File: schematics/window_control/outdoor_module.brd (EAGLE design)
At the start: 62.2 x 54.3 mm, 25 parts, among them J1 J_SMD, J10 USBASP_PIN, J2 J_SMD, J3 J_SMD, U5 BMP280 5V module, U6 LM317L, U7 LM358, U8 ATMEGA328P, U9 GY-SGP30

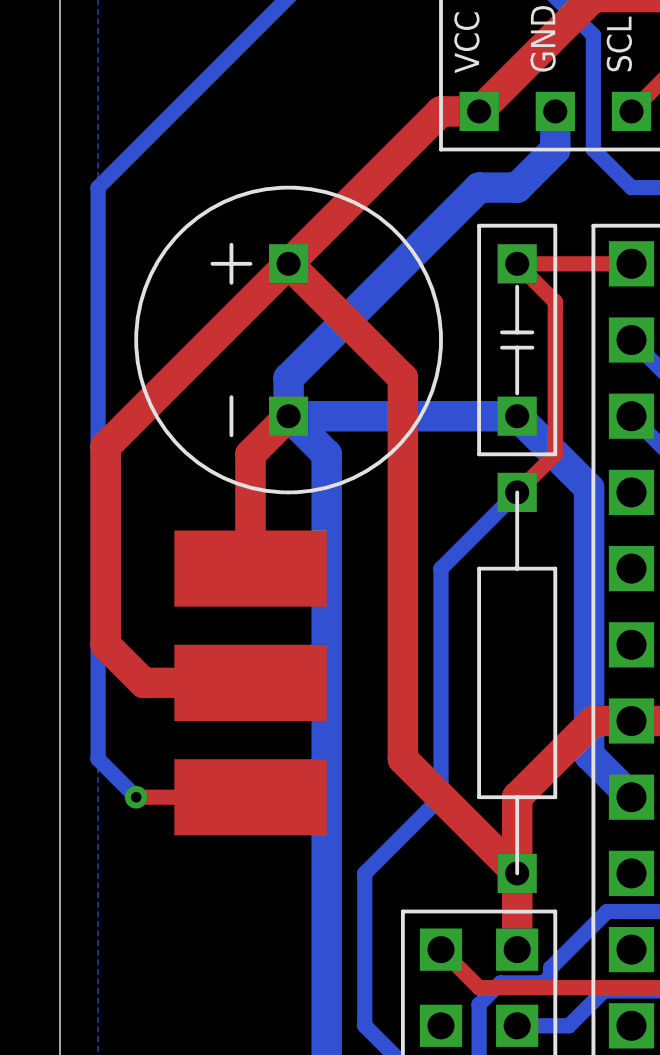
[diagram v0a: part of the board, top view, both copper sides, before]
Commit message: Connectors changed
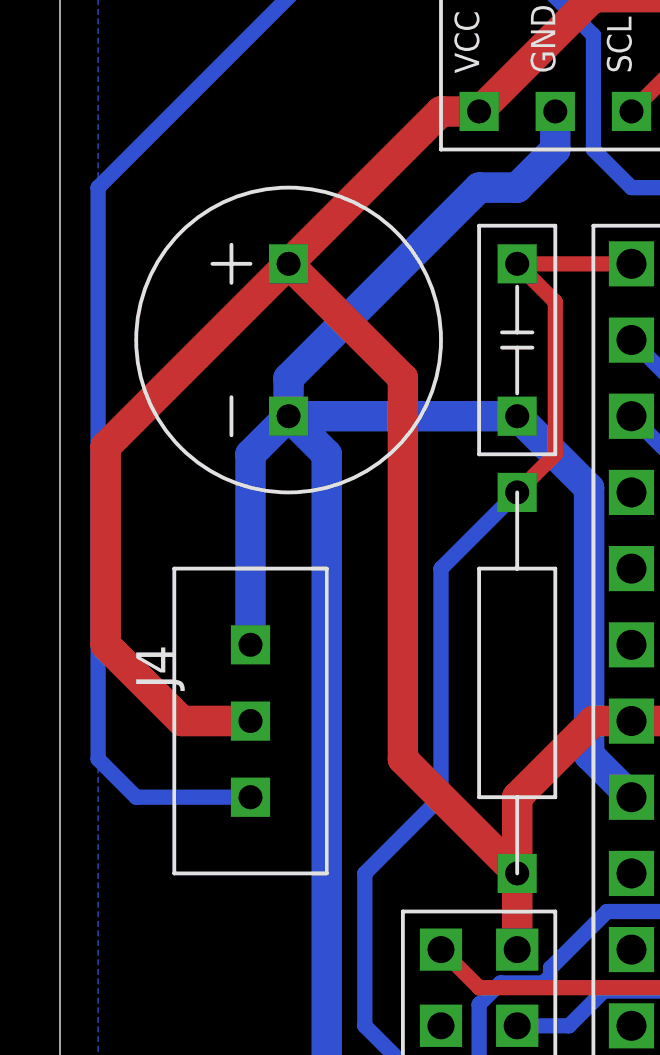
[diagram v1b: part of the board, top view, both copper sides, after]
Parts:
- removed J1, J2, J3: J_SMD, my_devices:J_SMD
- added J4: JST-XH2.54-3P, my_devices:JST-XH254-3P
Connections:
- net OUTDOOR_+5V: now also J4.PIN2; no longer J1.PIN
- net OUTDOOR_DATA_OUT: now also J4.PIN3; no longer J3.PIN
- net OUTDOOR_GND: now also J4.PIN1; no longer J2.PIN
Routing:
- net OUTDOOR_GND: track 216.7 -> 219.1 mm
- net OUTDOOR_+5V: track 121.1 -> 120.4 mm
- net OUTDOOR_DATA_OUT: track 63.4 -> 63.2 mm, vias 1 -> 0
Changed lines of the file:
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@@
 <drawing>
 <settings>
-<setting alwaysvectorfont="yes"/>
+<setting alwaysvectorfont="no"/>
 <setting verticaltext="up"/>
 </settings>
@@
 <element name="C8" library="my_devices" package="C-1" value="0.1 uF" x="124.46" y="-20.32" smashed="yes"/>
 <element name="C9" library="my_devices" package="C-1" value="0.1 uF" x="87.63" y="12.7" smashed="yes" rot="R90"/>
-<element name="J1" library="my_devices" package="J_SMD" value="J_SMD" x="78.74" y="1.27" smashed="yes"/>
 <element name="J10" library="my_devices" package="USBASP_PIN" value="USBASP_PIN" x="86.36" y="-12.7" smashed="yes"/>
-<element name="J2" library="my_devices" package="J_SMD" value="J_SMD" x="78.74" y="5.08" smashed="yes" rot="R180"/>
-<element name="J3" library="my_devices" package="J_SMD" value="J_SMD" x="78.74" y="-2.54" smashed="yes"/>
 <element name="L2" library="my_devices" package="L-EC24" value="EC24-561K, 560 uH" x="124.46" y="20.32" smashed="yes" rot="R270"/>
 <element name="L3" library="my_devices" package="L-EC24" value="EC24-561K, 560 uH" x="110.49" y="1.27" smashed="yes"/>
@@
 <element name="U8" library="my_devices" package="ATMEGA328P" value="ATMEGA328P" x="95.25" y="0" smashed="yes"/>
 <element name="U9" library="my_devices" package="GY-SGP30" value="GY-SGP30" x="106.68" y="20.32" smashed="yes" rot="R90"/>
+<element name="J4" library="my_devices" package="JST-XH254-3P" value="JST-XH2.54-3P" x="78.74" y="0" smashed="yes" rot="R270">
+<attribute name="NAME" x="74.93" y="2.54" size="1.27" layer="21" rot="R270"/>
+</element>
 </elements>
 <signals>
@@
 <contactref element="U5" pad="VCC"/>
 <contactref element="C6" pad="PIN_PLUS"/>
-<contactref element="J1" pad="PIN"/>
 <contactref element="L2" pad="P$1"/>
 <contactref element="U8" pad="AREF"/>
@@
 <contactref element="R21" pad="P$2"/>
 <contactref element="J10" pad="VCC"/>
-<wire x1="78.6384" y1="1.3716" x2="78.1812" y2="1.3716" width="0.1524" layer="1"/>
-<wire x1="78.6384" y1="1.3716" x2="78.74" y2="1.27" width="0.1524" layer="1"/>
 <wire x1="102.87" y1="20.4216" x2="102.87" y2="20.32" width="0.1524" layer="1"/>
-<wire x1="78.1812" y1="1.3716" x2="78.74" y2="1.27" width="0.1524" layer="1"/>
 <wire x1="124.46" y1="27.94" x2="120.65" y2="24.13" width="1.016" layer="1"/>
 <wire x1="120.65" y1="24.13" x2="105.41" y2="24.13" width="1.016" layer="1"/>
@@
 <wire x1="80.01" y1="15.24" x2="85.09" y2="20.32" width="1.016" layer="1"/>
 <wire x1="85.09" y1="20.32" x2="86.36" y2="20.32" width="1.016" layer="1"/>
-<wire x1="78.74" y1="1.27" x2="75.184" y2="1.27" width="1.016" layer="1"/>
-<wire x1="75.184" y1="1.27" x2="73.914" y2="2.54" width="1.016" layer="1"/>
-<wire x1="73.914" y1="2.54" x2="73.914" y2="9.144" width="1.016" layer="1"/>
+<wire x1="73.914" y1="9.144" x2="73.914" y2="2.54" width="1.016" layer="1"/>
 <wire x1="73.914" y1="9.144" x2="80.01" y2="15.24" width="1.016" layer="1"/>
 <wire x1="80.01" y1="15.24" x2="83.82" y2="11.43" width="1.016" layer="1"/>
@@
 <wire x1="99.06" y1="-2.54" x2="99.06" y2="-5.08" width="1.016" layer="1"/>
 <wire x1="87.63" y1="-7.62" x2="87.63" y2="-5.08" width="1.016" layer="1"/>
+<contactref element="J4" pad="PIN2"/>
+<wire x1="76.454" y1="0" x2="78.74" y2="0" width="1.016" layer="1"/>
+<wire x1="73.914" y1="2.54" x2="76.454" y2="0" width="1.016" layer="1"/>
 </signal>
 <signal name="OUTDOOR_GND">
@@
 <contactref element="U9" pad="GND"/>
 <contactref element="C6" pad="PIN_GND"/>
-<contactref element="J2" pad="PIN"/>
 <contactref element="BM1" pad="P$1"/>
 <contactref element="U7" pad="PIN_4"/>
@@
 <contactref element="J10" pad="GND"/>
 <contactref element="J10" pad="GND1"/>
-<wire x1="78.7908" y1="5.1816" x2="78.74" y2="5.08" width="0.1524" layer="1"/>
 <wire x1="105.3084" y1="20.2692" x2="105.41" y2="20.32" width="0.1524" layer="16"/>
 <wire x1="123.19" y1="-5.08" x2="121.92" y2="-3.81" width="1.016" layer="16"/>
@@
 <wire x1="120.65" y1="11.43" x2="120.65" y2="12.7" width="1.016" layer="16"/>
 <wire x1="120.65" y1="12.7" x2="116.84" y2="16.51" width="1.016" layer="16"/>
-<wire x1="78.74" y1="5.08" x2="78.74" y2="8.89" width="1.016" layer="1"/>
-<wire x1="78.74" y1="8.89" x2="80.01" y2="10.16" width="1.016" layer="1"/>
 <wire x1="80.01" y1="10.16" x2="87.63" y2="10.16" width="1.016" layer="16"/>
 <wire x1="80.01" y1="10.16" x2="80.01" y2="11.43" width="1.016" layer="16"/>
@@
 <vertex x="73.66" y="-22.86"/>
 </polygon>
+<contactref element="J4" pad="PIN1"/>
+<wire x1="80.01" y1="10.16" x2="78.74" y2="8.89" width="1.016" layer="16"/>
+<wire x1="78.74" y1="8.89" x2="78.74" y2="2.54" width="1.016" layer="16"/>
 </signal>
 <signal name="I2C_SDA">
@@
 </signal>
 <signal name="OUTDOOR_DATA_OUT">
-<contactref element="J3" pad="PIN"/>
 <contactref element="U8" pad="PC3"/>
-<wire x1="78.7908" y1="-2.4384" x2="78.74" y2="-2.54" width="0.1524" layer="1"/>
-<wire x1="78.74" y1="-2.54" x2="74.93" y2="-2.54" width="0.508" layer="1"/>
-<via x="74.93" y="-2.54" extent="1-16" drill="0.35"/>
-<wire x1="74.93" y1="-2.54" x2="73.66" y2="-1.27" width="0.508" layer="16"/>
 <wire x1="73.66" y1="17.78" x2="81.28" y2="25.4" width="0.508" layer="16"/>
 <wire x1="81.28" y1="25.4" x2="87.63" y2="25.4" width="0.508" layer="16"/>
@@
 <wire x1="92.71" y1="17.78" x2="95.25" y2="15.24" width="0.508" layer="16"/>
 <wire x1="95.25" y1="15.24" x2="95.25" y2="12.7" width="0.508" layer="16"/>
-<wire x1="73.66" y1="-1.27" x2="73.66" y2="17.78" width="0.508" layer="16"/>
+<wire x1="73.66" y1="17.78" x2="73.66" y2="-1.27" width="0.508" layer="16"/>
 <wire x1="95.25" y1="12.7" x2="97.79" y2="10.16" width="0.508" layer="16"/>
 <wire x1="97.79" y1="10.16" x2="99.06" y2="10.16" width="0.508" layer="16"/>
@@
 <wire x1="90.17" y1="19.05" x2="91.44" y2="17.78" width="0.508" layer="16"/>
 <wire x1="91.44" y1="17.78" x2="92.71" y2="17.78" width="0.508" layer="16"/>
+<contactref element="J4" pad="PIN3"/>
+<wire x1="73.66" y1="-1.27" x2="74.93" y2="-2.54" width="0.508" layer="16"/>
+<wire x1="74.93" y1="-2.54" x2="78.74" y2="-2.54" width="0.508" layer="16"/>
 </signal>
 <signal name="N$17">

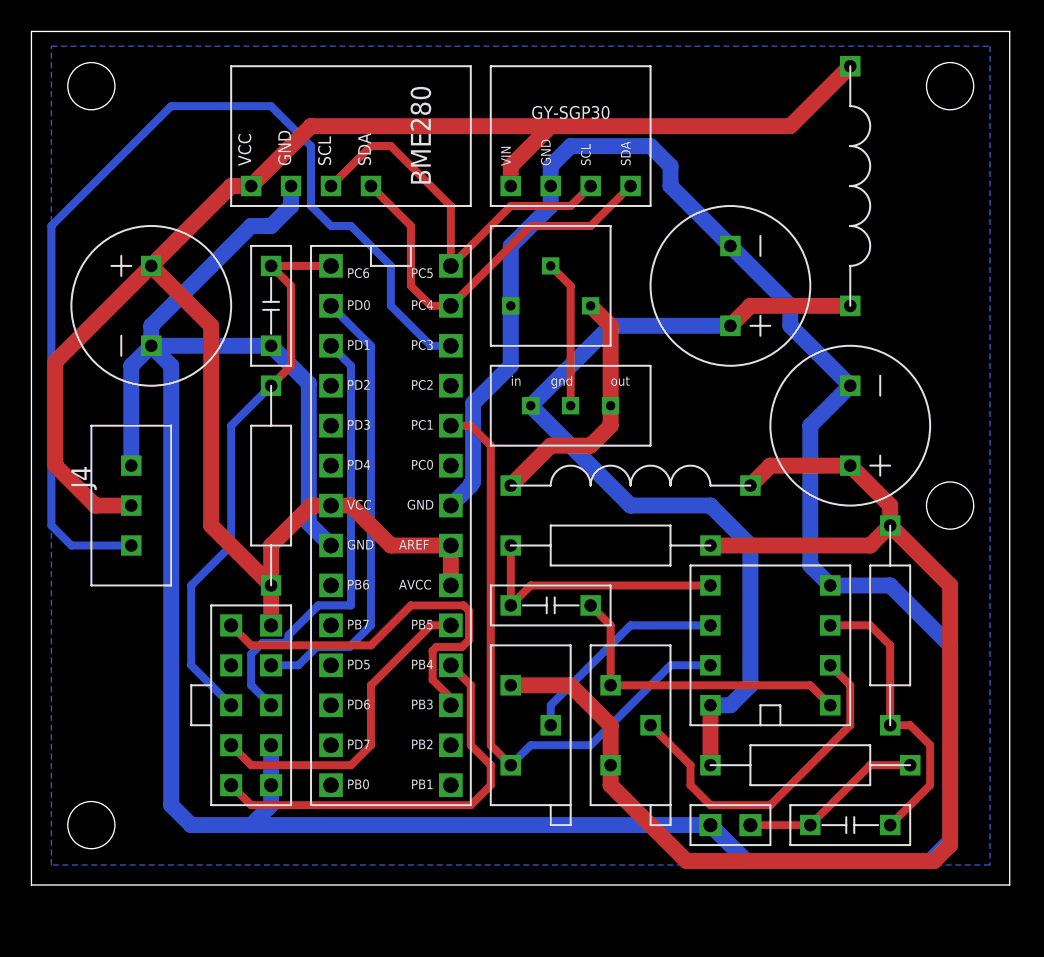
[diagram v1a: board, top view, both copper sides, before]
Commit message: Outdoor module board size reduced
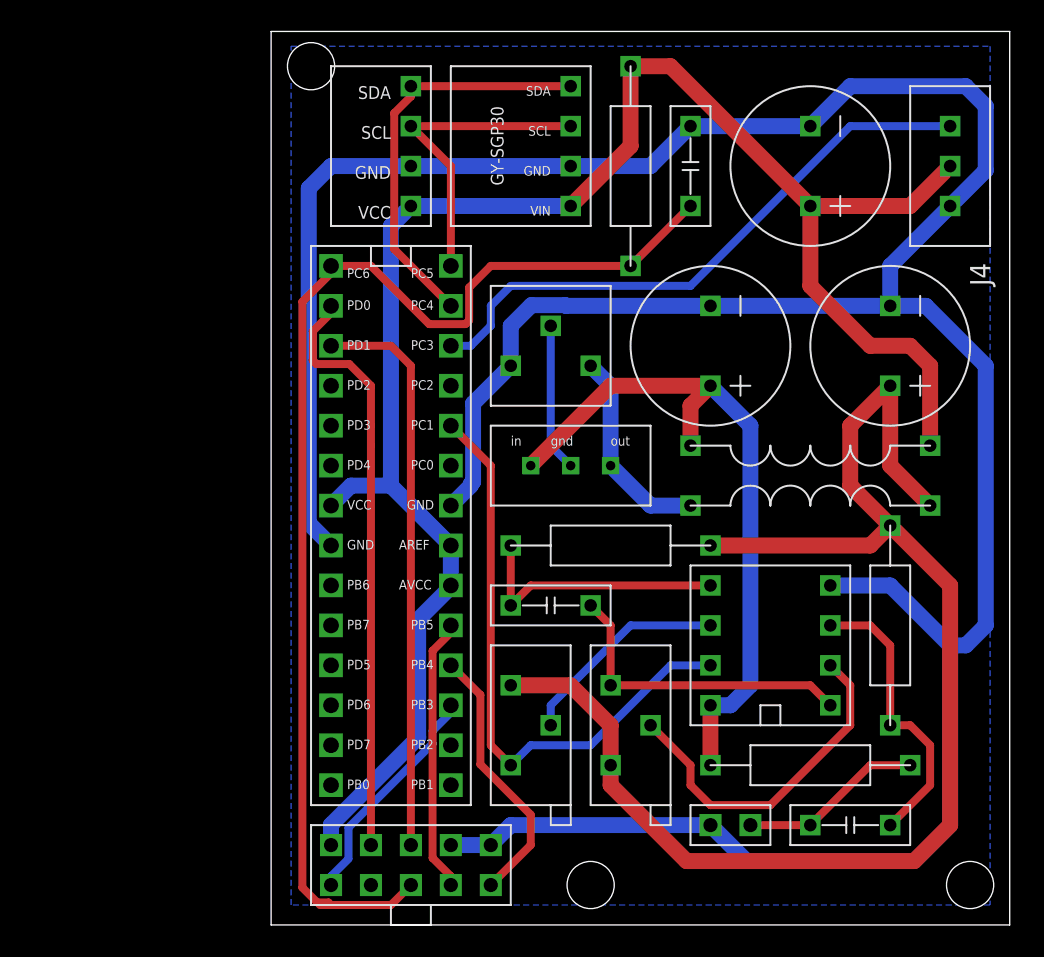
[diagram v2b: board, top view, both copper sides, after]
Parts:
- U5: device my_devices:BME280 -> my_devices:BME280-CONNECTOR-ONLY
- moved J4 56.4 mm to (130.8, 21.6), turned to 90 degrees
- moved C6 42.8 mm to (121.9, 21.6), turned to 90 degrees
- moved R21 30.6 mm to (110.5, 21.6), turned to 90 degrees
- moved C9 28.1 mm to (114.3, 21.6), turned to 270 degrees
- moved L2 16.7 mm to (121.9, 3.81), turned to 180 degrees
- moved J10 14.4 mm to (96.5, -22.9), turned to 90 degrees
- moved L3 11.5 mm to (121.9, 0.00)
- moved C10 5.68 mm to (127.0, 10.2)
- moved C7 4.02 mm to (115.6, 10.2)
- moved R17 3.81 mm to (105.4, 10.2)
- moved U6 3.81 mm to (106.7, 2.54)
- moved U5 2.84 mm to (91.4, 22.9), turned to 180 degrees
- moved U9 2.54 mm to (106.7, 22.9), turned to 180 degrees
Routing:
- net ATMEGA_RESET: track 36.0 -> 77.6 mm
- net OUTDOOR_DATA_OUT: track 63.2 -> 38.3 mm
- net OUTDOOR_GND: track 219.1 -> 204.2 mm
- net OUTDOOR_+5V_F: track 56.4 -> 44.8 mm
- net N$24: track 25.2 -> 14.6 mm
- net N$25: track 26.2 -> 17.1 mm
- net ATMEGA_TXD: track 28.8 -> 37.5 mm
- net ATMEGA_RXD: track 28.6 -> 36.1 mm
- net OUTDOOR_MIDDLEPOINT: track 80.8 -> 88.0 mm
- net I2C_SCL: track 25.1 -> 20.1 mm
- net OUTDOOR_+5V: track 120.4 -> 115.8 mm
- net OUT: track 16.1 -> 13.0 mm
- net N$26: track 20.4 -> 17.5 mm
- net I2C_SDA: track 25.1 -> 26.1 mm
- net NOISE_LEVEL: track 39.2 -> 38.5 mm
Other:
- board size 62.2 x 54.3 mm -> 47 x 56.8 mm

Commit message: Start preparing to order boards. Checked all labels
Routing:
- net ATMEGA_RESET: track 77.6 -> 76.8 mm
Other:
- board text added: "+5V"
- board text added: "BM1"
- board text added: "C10"
- board text added: "C11"
- board text added: "C6"
- board text added: "C7"
- board text added: "C8"
- board text added: "C9"
- board text added: "GND"
- board text added: "J10"
- board text added: "L2"
- board text added: "L3"
- board text added: "R17"
- board text added: "R18"
- board text added: "R19"
- board text added: "R20"
- board text added: "R21"
- board text added: "R22"
- board text added: "R23"
- board text added: "SGN"
- board text added: "U5"
- board text added: "U7"
- board text added: "U8"
- board text added: "U9"
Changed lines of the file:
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@@
 <hole x="132.08" y="-24.13" drill="3"/>
 <hole x="107.95" y="-24.13" drill="3"/>
+<text x="119.38" y="15.24" size="1.27" layer="21">C6</text>
+<text x="115.57" y="16.51" size="1.27" layer="21">C9</text>
+<text x="111.76" y="27.94" size="1.27" layer="21">R21</text>
+<text x="105.41" y="15.24" size="1.27" layer="21">U9</text>
+<text x="88.9" y="24.13" size="1.27" layer="21">U5</text>
+<text x="100.33" y="15.24" size="1.27" layer="21">U8</text>
+<text x="109.22" y="5.08" size="1.27" layer="21">R17</text>
+<text x="120.65" y="6.35" size="1.27" layer="21">C7</text>
+<text x="130.81" y="5.08" size="1.27" layer="21">C10</text>
+<text x="130.81" y="2.54" size="1.27" layer="21">L2</text>
+<text x="130.81" y="-1.27" size="1.27" layer="21">L3</text>
+<text x="116.84" y="-2.54" size="1.27" layer="21">R22</text>
+<text x="109.22" y="-6.35" size="1.27" layer="21">C11</text>
+<text x="121.92" y="-3.81" size="1.27" layer="21">U7</text>
+<text x="128.27" y="-7.62" size="1.27" layer="21">R19</text>
+<text x="129.54" y="-16.51" size="1.27" layer="21">R18</text>
+<text x="125.73" y="-22.86" size="1.27" layer="21">C8</text>
+<text x="115.57" y="-22.86" size="1.27" layer="21">BM1</text>
+<text x="110.49" y="-21.59" size="1.27" layer="21">R20</text>
+<text x="104.14" y="-21.59" size="1.27" layer="21">R23</text>
+<text x="102.87" y="-24.13" size="1.27" layer="21">J10</text>
+<text x="129.54" y="17.78" size="1.778" layer="26" rot="MR0">GND</text>
+<text x="129.54" y="20.32" size="1.778" layer="26" rot="MR0">+5V</text>
+<text x="129.54" y="22.86" size="1.778" layer="26" rot="MR0">SGN</text>
 </plain>
 <attributes>
@@
 <element name="U9" library="my_devices" package="GY-SGP30" value="GY-SGP30" x="106.68" y="22.86" smashed="yes" rot="R180"/>
 <element name="J4" library="my_devices" package="JST-XH254-3P" value="JST-XH2.54-3P" x="130.81" y="21.59" smashed="yes" rot="R90">
-<attribute name="NAME" x="133.35" y="13.97" size="1.27" layer="21" rot="R90"/>
+<attribute name="NAME" x="133.35" y="15.24" size="1.27" layer="21" rot="R180"/>
 </element>
 </elements>
@@
 <contactref element="U7" pad="PIN_6"/>
 <contactref element="R23" pad="P3"/>
-<wire x1="105.4608" y1="-13.8684" x2="105.41" y2="-13.97" width="0.1524" layer="1"/>
 <wire x1="105.41" y1="-13.97" x2="105.41" y2="-12.7" width="0.508" layer="16"/>
 <wire x1="110.49" y1="-7.62" x2="115.57" y2="-7.62" width="0.508" layer="16"/>
@@
 <wire x1="101.6" y1="15.24" x2="110.49" y2="15.24" width="0.508" layer="1"/>
 <wire x1="110.49" y1="15.24" x2="114.3" y2="19.05" width="0.508" layer="1"/>
-<wire x1="96.52" y1="-24.13" x2="95.25" y2="-25.4" width="0.508" layer="1"/>
-<wire x1="95.25" y1="-25.4" x2="91.44" y2="-25.4" width="0.508" layer="1"/>
-<wire x1="91.44" y1="-25.4" x2="90.7272625" y2="-25.4" width="0.508" layer="1"/>
 <wire x1="100.2204" y1="11.7776625" x2="99.9823375" y2="11.5396" width="0.508" layer="1"/>
 <wire x1="99.9823375" y1="11.5396" x2="97.6804" y2="11.5396" width="0.508" layer="1"/>
 <wire x1="97.6804" y1="11.5396" x2="93.98" y2="15.24" width="0.508" layer="1"/>
-<wire x1="91.44" y1="-25.4" x2="91.2804" y2="-25.2404" width="0.508" layer="1"/>
-<wire x1="91.2804" y1="-25.2404" x2="90.5676625" y2="-25.2404" width="0.508" layer="1"/>
 <wire x1="91.44" y1="14.7827375" x2="91.44" y2="15.24" width="0.508" layer="1"/>
 <wire x1="89.6192" y1="12.9619375" x2="91.44" y2="14.7827375" width="0.508" layer="1"/>
-<wire x1="90.5676625" y1="-25.2404" x2="89.6192" y2="-24.2919375" width="0.508" layer="1"/>
+<wire x1="89.6192" y1="-24.2919375" x2="90.5676625" y2="-25.2404" width="0.508" layer="1"/>
 <wire x1="89.6192" y1="-24.2919375" x2="89.6192" y2="12.9619375" width="0.508" layer="1"/>
+<wire x1="95.4096" y1="-25.2404" x2="96.52" y2="-24.13" width="0.508" layer="1"/>
+<wire x1="90.5676625" y1="-25.2404" x2="95.4096" y2="-25.2404" width="0.508" layer="1"/>
 </signal>
 <signal name="ATMEGA_TXD">

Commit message: Holes moved away from board border
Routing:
- net OUTDOOR_GND: track 204.2 -> 205.3 mm
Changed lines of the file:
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@@
 <drawing>
 <settings>
-<setting alwaysvectorfont="yes"/>
+<setting alwaysvectorfont="no"/>
 <setting verticaltext="up"/>
 </settings>
@@
 <wire x1="134.6" y1="30.15" x2="87.63" y2="30.15" width="0" layer="20"/>
 <wire x1="87.63" y1="30.15" x2="87.63" y2="-26.67" width="0" layer="20"/>
-<hole x="90.17" y="27.94" drill="3"/>
+<hole x="91.44" y="26.67" drill="3"/>
 <hole x="132.08" y="-24.13" drill="3"/>
-<hole x="107.95" y="-24.13" drill="3"/>
+<hole x="109.22" y="-22.86" drill="3"/>
 <text x="119.38" y="15.24" size="1.27" layer="21">C6</text>
 <text x="115.57" y="16.51" size="1.27" layer="21">C9</text>
@@
 <wire x1="90.0256" y1="-1.1256" x2="91.44" y2="-2.54" width="1.016" layer="16"/>
 <wire x1="91.44" y1="21.59" x2="90.0256" y2="20.1756" width="1.016" layer="16"/>
-<wire x1="101.6" y1="-21.59" x2="102.87" y2="-20.32" width="1.016" layer="16"/>
-<wire x1="102.87" y1="-20.32" x2="115.57" y2="-20.32" width="1.016" layer="16"/>
 <wire x1="117.856" y1="-22.606" x2="128.524" y2="-22.606" width="1.016" layer="16"/>
 <wire x1="130.81" y1="-20.32" x2="130.81" y2="-8.89" width="1.016" layer="16"/>
@@
 <vertex x="88.9" y="-25.4"/>
 </polygon>
+<wire x1="114.3" y1="-19.05" x2="115.57" y2="-20.32" width="1.016" layer="16"/>
+<wire x1="101.6" y1="-21.59" x2="104.14" y2="-19.05" width="1.016" layer="16"/>
+<wire x1="104.14" y1="-19.05" x2="114.3" y2="-19.05" width="1.016" layer="16"/>
 </signal>
 <signal name="I2C_SDA">
